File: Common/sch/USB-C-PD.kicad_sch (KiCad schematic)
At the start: 33 parts, among them J201 USB_C_Receptacle_USB2.0_16P, Q201 IRF9358, Q202 2N7002, Q203 BSL308PE, U201 USBLC6-2SC6, U202 CYPD3177-24LQ

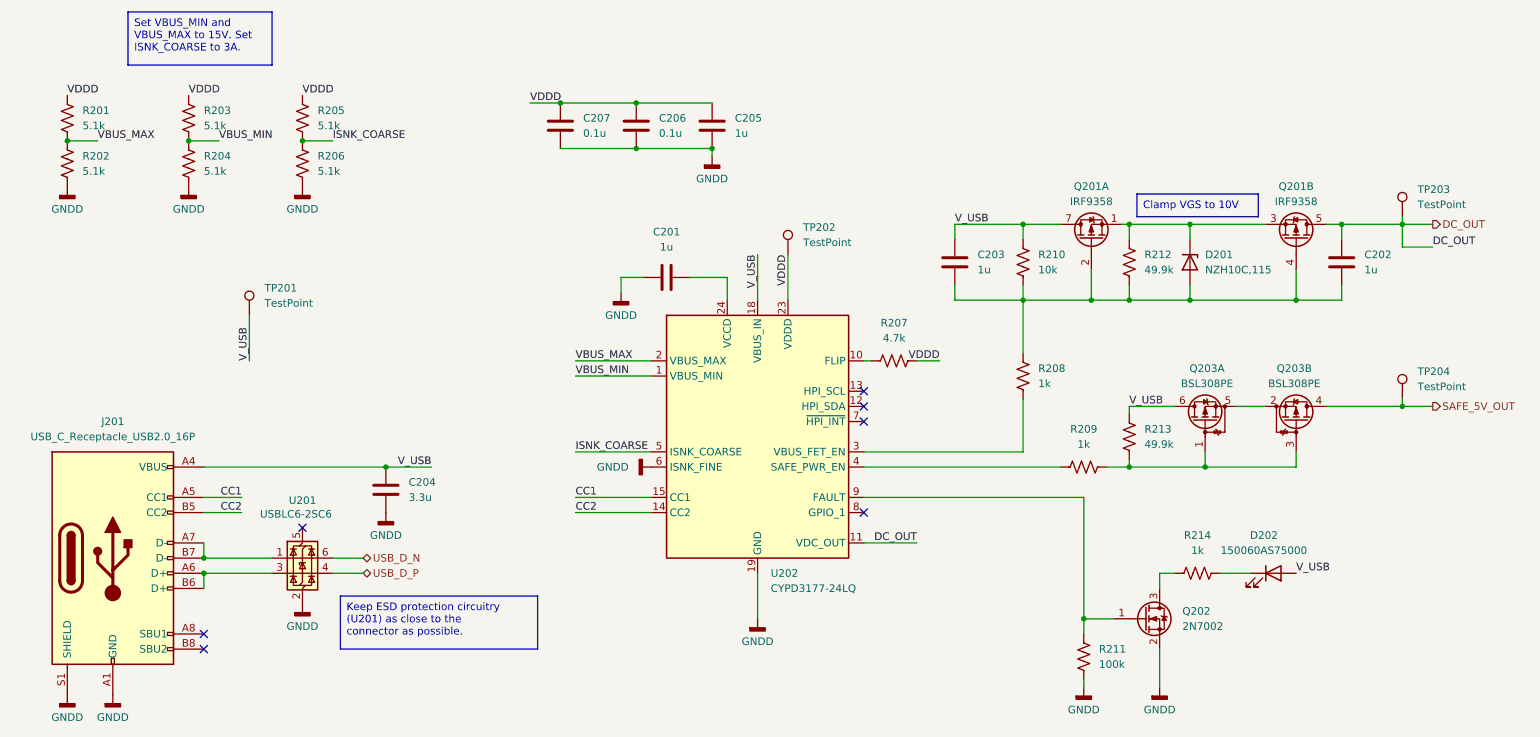
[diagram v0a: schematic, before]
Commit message: USB-C PD Controller finishing touches
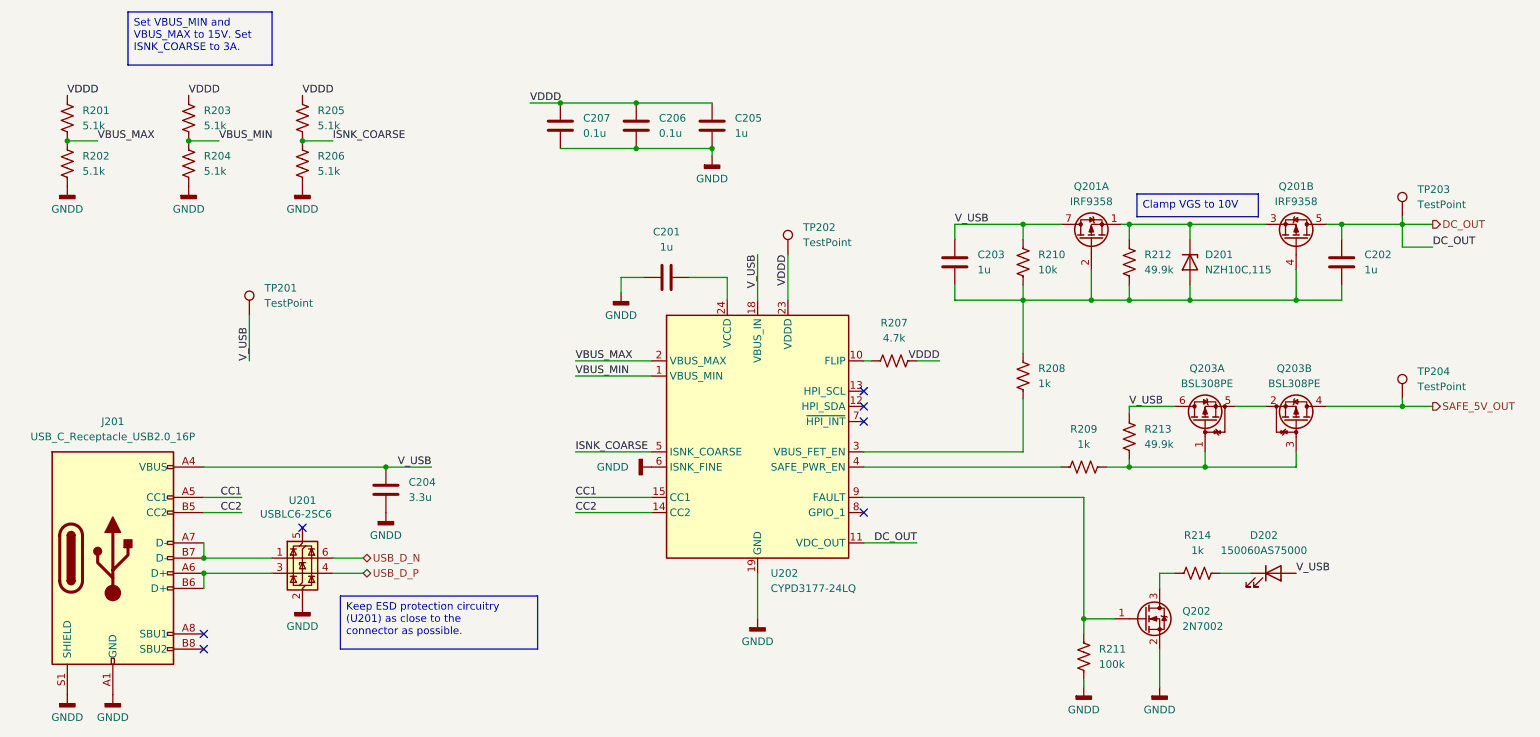
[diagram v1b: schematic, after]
